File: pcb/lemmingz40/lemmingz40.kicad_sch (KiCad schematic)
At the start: 107 parts, among them J1 USB_C_Receptacle_USB2.0, SW1 RST, SW1 SW_Push, SW10 SW_Push, SW11 SW_Push, SW12 SW_Push, SW13 SW_Push, SW14 SW_Push, SW15 SW_Push, SW16 SW_Push, SW17 SW_Push, SW18 SW_Push, SW19 SW_Push, SW2 RST, SW2 SW_Push, SW20 SW_Push, SW21 SW_Push, SW22 SW_Push, SW23 SW_Push, SW24 SW_Push, SW25 SW_Push, SW26 SW_Push, SW27 SW_Push, SW28 SW_Push, SW29 SW_Push, SW3 SW_Push, SW30 SW_Push, SW31 SW_Push, SW32 SW_Push, SW33 SW_Push, SW34 SW_Push, SW35 SW_Push, SW36 SW_Push, SW37 SW_Push, SW38 SW_Push, SW39 SW_Push, SW4 SW_Push, SW40 SW_Push, SW5 SW_Push, SW6 SW_Push, SW7 SW_Push, SW8 SW_Push, SW9 SW_Push, U1 USBLC6-2SC6, U2 STM32F072C8Tx, U3 XC6206PxxxMR-Regulator_Linear

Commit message: add v0.0 exports
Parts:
- removed H1, H2, H3, H4, H5, H6, H7, H8: MountingHole, userlib:m1.6_hole, symbol Mechanical:MountingHole
- removed J1: USB_C_Receptacle_USB2.0, Connector_USB:USB_C_Receptacle_XKB_U262-16XN-4BVC11, symbol Connector:USB_C_Receptacle_USB2.0
- added H1, H2, H3, H4, H5, H6, H7, H8: MountingHole_Pad, userlib:SMTSO-M1.6, symbol Mechanical:MountingHole_Pad
- added J1: USB2_C_Receptacle, userlib:Mid_Mount-USB_C, symbol usb-type-c:USB2_C_Receptacle
- SW2: value RST -> BOOT
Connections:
- net COL0 is gone; now on net ROW1: U2.30 (PA9)
- net COL1: now also U2.22 (PB11); no longer U2.29 (PA8)
- net COL10: now also U2.6 (PF1); no longer U2.15 (PA5)
- net COL2: now also U2.2 (PC13); no longer U2.28 (PB15)
- net COL3: now also U2.21 (PB10); no longer U2.27 (PB14)
- net COL4: now also U2.3 (PC14); no longer U2.26 (PB13)
- net COL5: now also U2.20 (PB2); no longer U2.25 (PB12)
- net COL6: now also U2.4 (PC15); no longer U2.18 (PB0)
- net COL7: now also U2.19 (PB1); no longer U2.39 (PB3)
- net COL8: now also U2.5 (PF0); no longer U2.17 (PA7)
- net COL9: now also U2.18 (PB0); no longer U2.16 (PA6)
- net D_USB_+: now also J1.A7 (D-), J1.B7 (D-)
- net D_USB_-: now also J1.A6 (D+), J1.B6 (D+)
- net GND: now also H1.1, H2.1, H3.1, H4.1, H5.1, H6.1, H7.1, H8.1, J1.A1B12 (GND), J1.B1A12 (GND), J1.S1 (Shield)
- net ROW1: no longer U2.37 (PA14)
- net ROW2: now also U2.29 (PA8); no longer U2.22 (PB11)
- net ROW3: now also U2.28 (PB15); no longer U2.21 (PB10)
- net ROW4: now also U2.27 (PB14)
- net VBUS: now also J1.A4B9 (VBUS), J1.B4A9 (VBUS)
- net at R1.2: now also J1.B5 (CC2)
- net at R1.1: now also J1.A5 (CC1)
- net LED_SLCK: no longer names the net of U2.40 (PB4)
- net ROW0: no longer names the net of U2.38 (PA15)
- no-connect marks 2 -> 21
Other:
- moved on the sheet: R1

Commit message: add exports and photos
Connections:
- net +5V: now also U1.5 (VBUS)
- net VBUS: no longer U1.5 (VBUS)
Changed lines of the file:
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@@
-    )
-  )
-  (symbol (lib_id "power:VBUS") (at 104.14 21.59 0) (unit 1)
-    (in_bom yes) (on_board yes) (dnp no) (fields_autoplaced)
-    (property "Reference" "#PWR02" (at 104.14 25.4 0)
-      (effects (font (size 1.27 1.27)) hide)
-    )
-    (property "Value" "VBUS" (at 104.14 16.51 0)
-      (effects (font (size 1.27 1.27)))
-    )
-    (property "Footprint" "" (at 104.14 21.59 0)
-      (effects (font (size 1.27 1.27)) hide)
-    )
-    (property "Datasheet" "" (at 104.14 21.59 0)
-      (effects (font (size 1.27 1.27)) hide)
-    )
-    (pin "1")
-    (instances
-      (project ""
-        (path "/4811c7b7-222c-4bb6-b7b5-b7dd4d2eb234"
-          (reference "#PWR02") (unit 1)
-        )
-      )
-      (project "lemmingz40"
-        (path "/e63e39d7-6ac0-4ffd-8aa3-1841a4541b55"
-          (reference "#PWR02") (unit 1)
-        )
-      )
     )
   )
@@
         )
       )
+    )
+  )
+  (symbol (lib_id "power:+5V") (at 104.14 21.59 0) (unit 1)
+    (in_bom yes) (on_board yes) (dnp no) (fields_autoplaced)
+    (property "Reference" "#PWR04" (at 104.14 25.4 0)
+      (effects (font (size 1.27 1.27)) hide)
+    )
+    (property "Value" "+5V" (at 104.14 16.51 0)
+      (effects (font (size 1.27 1.27)))
+    )
+    (property "Footprint" "" (at 104.14 21.59 0)
+      (effects (font (size 1.27 1.27)) hide)
+    )
+    (property "Datasheet" "" (at 104.14 21.59 0)
+      (effects (font (size 1.27 1.27)) hide)
+    )
+    (pin "1")
+    (instances
+      (project ""
+        (path "/4811c7b7-222c-4bb6-b7b5-b7dd4d2eb234"
+          (reference "#PWR04") (unit 1)
+        )
+      )
+      (project "lemmingz40"
+        (path "/e63e39d7-6ac0-4ffd-8aa3-1841a4541b55"
+          (reference "#PWR02") (unit 1)
+        )
+      )

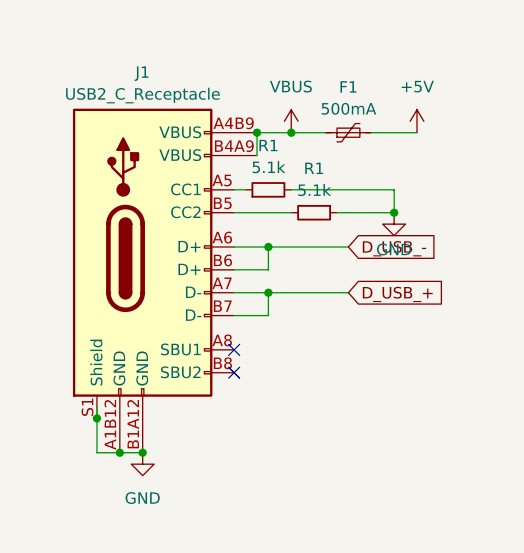
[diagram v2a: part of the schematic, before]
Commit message: update serial wire error, make standoffs 2mm from 1.5mm
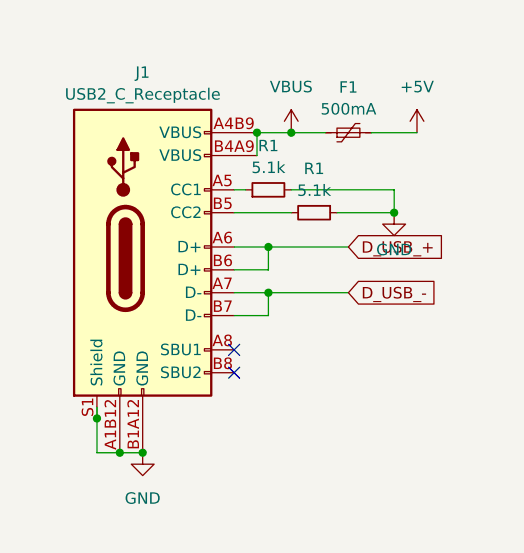
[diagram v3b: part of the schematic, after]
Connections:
- net D_USB_+: now also J1.A6 (D+), J1.B6 (D+); no longer J1.A7 (D-), J1.B7 (D-)
- net D_USB_-: now also J1.A7 (D-), J1.B7 (D-); no longer J1.A6 (D+), J1.B6 (D+)
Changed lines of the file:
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@@
     )
   )
-  (global_label "D_USB_-" (shape input) (at 215.9 40.64 0) (fields_autoplaced)
+  (global_label "D_USB_+" (shape input) (at 215.9 40.64 0) (fields_autoplaced)
     (effects (font (size 1.27 1.27)) (justify left))
-    (property "Intersheetrefs" "${INTERSHEET_REFS}" (at 226.9007 40.5606 0)
+    (property "Intersheetrefs" "${INTERSHEET_REFS}" (at 227.4728 40.64 0)
       (effects (font (size 1.27 1.27)) (justify left) hide)
     )
@@
     )
   )
-  (global_label "D_USB_+" (shape input) (at 215.9 45.72 0) (fields_autoplaced)
+  (global_label "D_USB_-" (shape input) (at 215.9 45.72 0) (fields_autoplaced)
     (effects (font (size 1.27 1.27)) (justify left))
-    (property "Intersheetrefs" "${INTERSHEET_REFS}" (at 226.9007 45.6406 0)
+    (property "Intersheetrefs" "${INTERSHEET_REFS}" (at 227.4728 45.72 0)
       (effects (font (size 1.27 1.27)) (justify left) hide)
     )
